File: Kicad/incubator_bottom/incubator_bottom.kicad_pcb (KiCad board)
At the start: 2 copper layers, 100.1 x 73.7 mm, 38 parts, among them J1 Conn_01x02, J2 Conn_02x03_Odd_Even, J3 RJ12, J4 Conn_01x05, J5 AudioJack3_SwitchTR, J6 AudioJack3_SwitchTR, J7 Conn_01x02, J8 Conn_01x06, Q1 ZXMS6004, Q2 IPB80N03S4L-03, U1 DS18B20Z, U2 DS18B20, U3 ATmega328P-AU

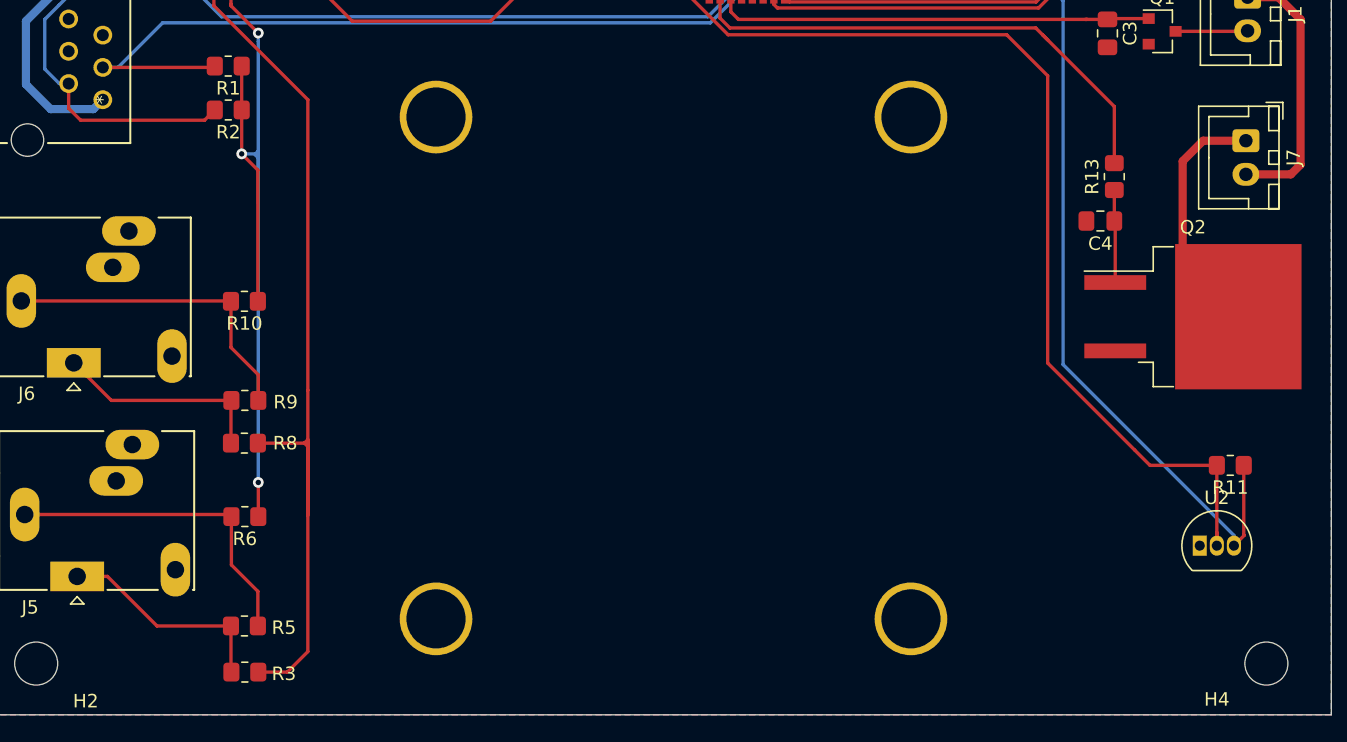
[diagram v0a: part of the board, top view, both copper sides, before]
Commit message: fix: Power resistor size
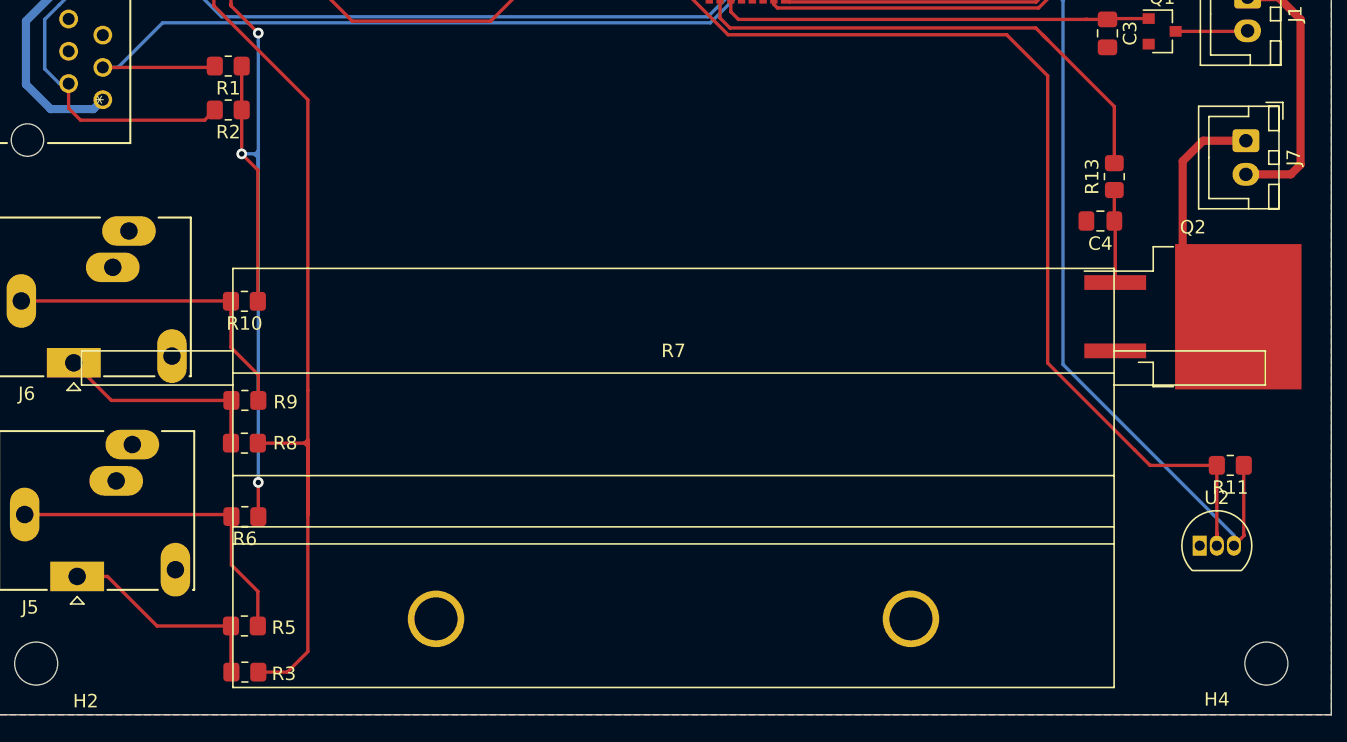
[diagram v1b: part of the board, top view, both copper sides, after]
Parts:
- R7: footprint Incubator:HSC1004R0J -> Incubator:100W4RJ; moved to F.Cu

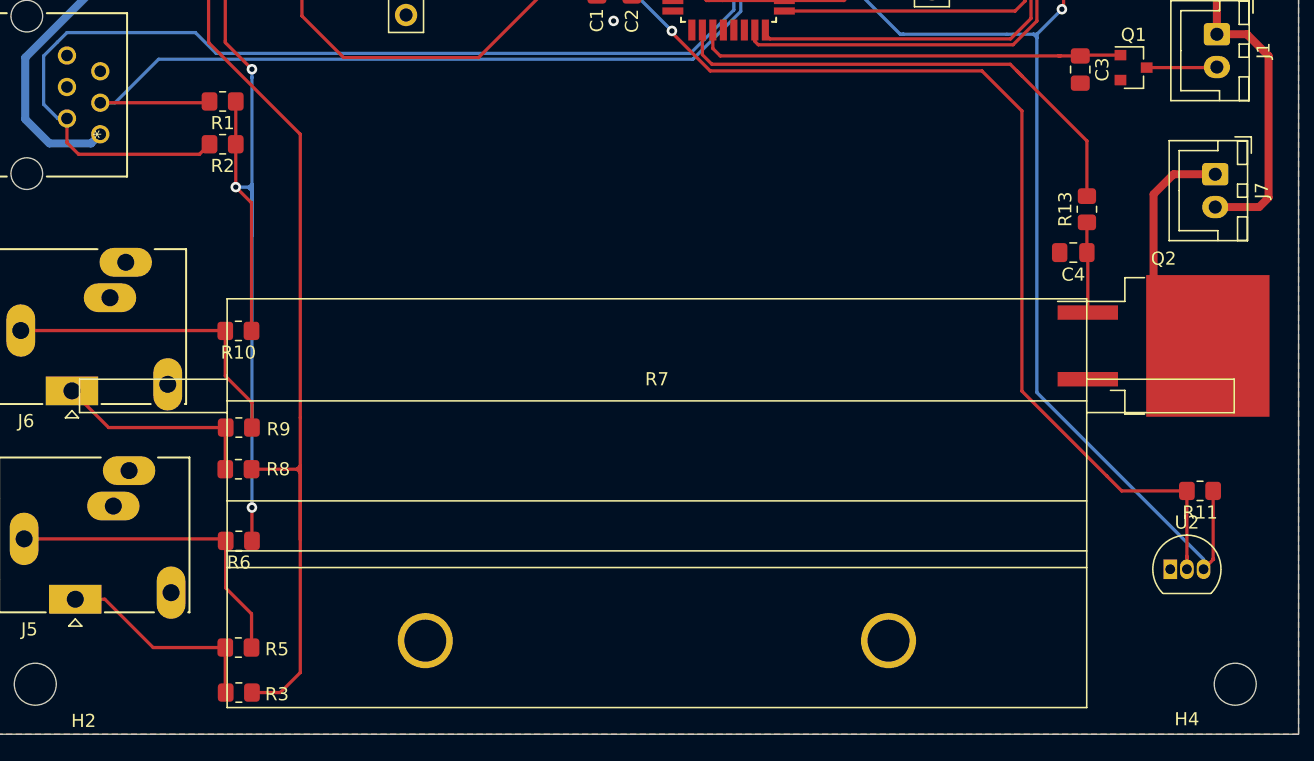
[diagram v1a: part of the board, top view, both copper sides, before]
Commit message: fix: Power resistor size and position
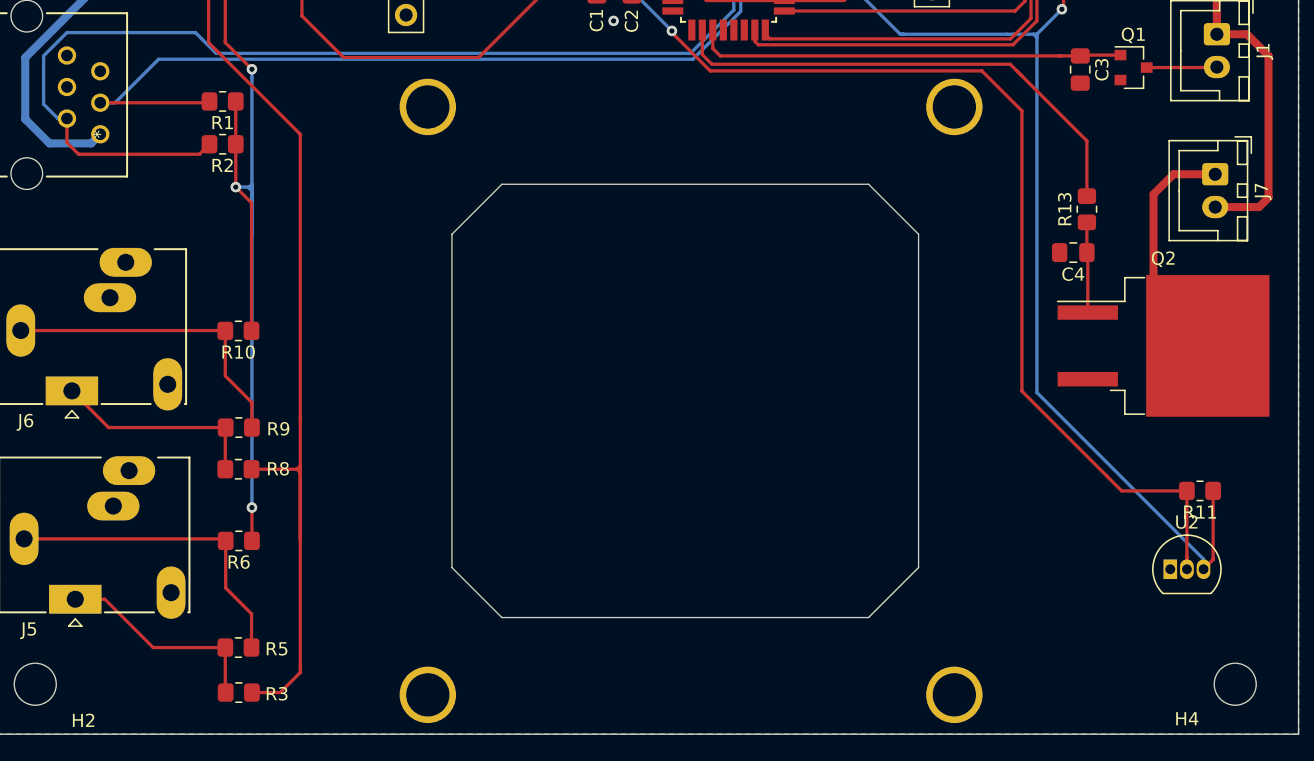
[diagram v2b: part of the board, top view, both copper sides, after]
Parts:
- added R15: 100W4RJ, Incubator:100W4RJ, B.Cu at (63.2, -25.4)
- R7: value HSC1004R0J -> 100W4RJ; moved to B.Cu
- moved R7 6.87 mm to (44.3, -25.4), turned to 90 degrees
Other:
- outline, holes or cut-outs redrawn

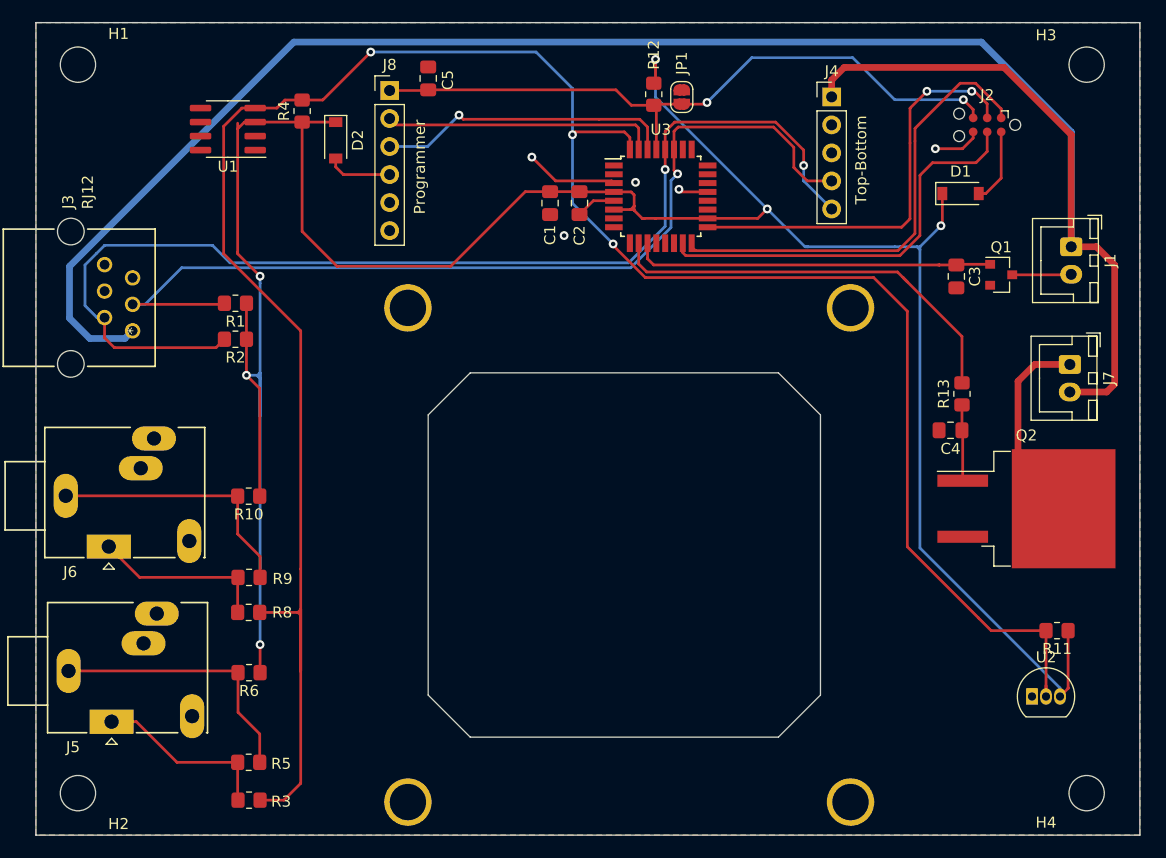
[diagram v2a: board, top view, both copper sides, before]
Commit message: fix: fan connection
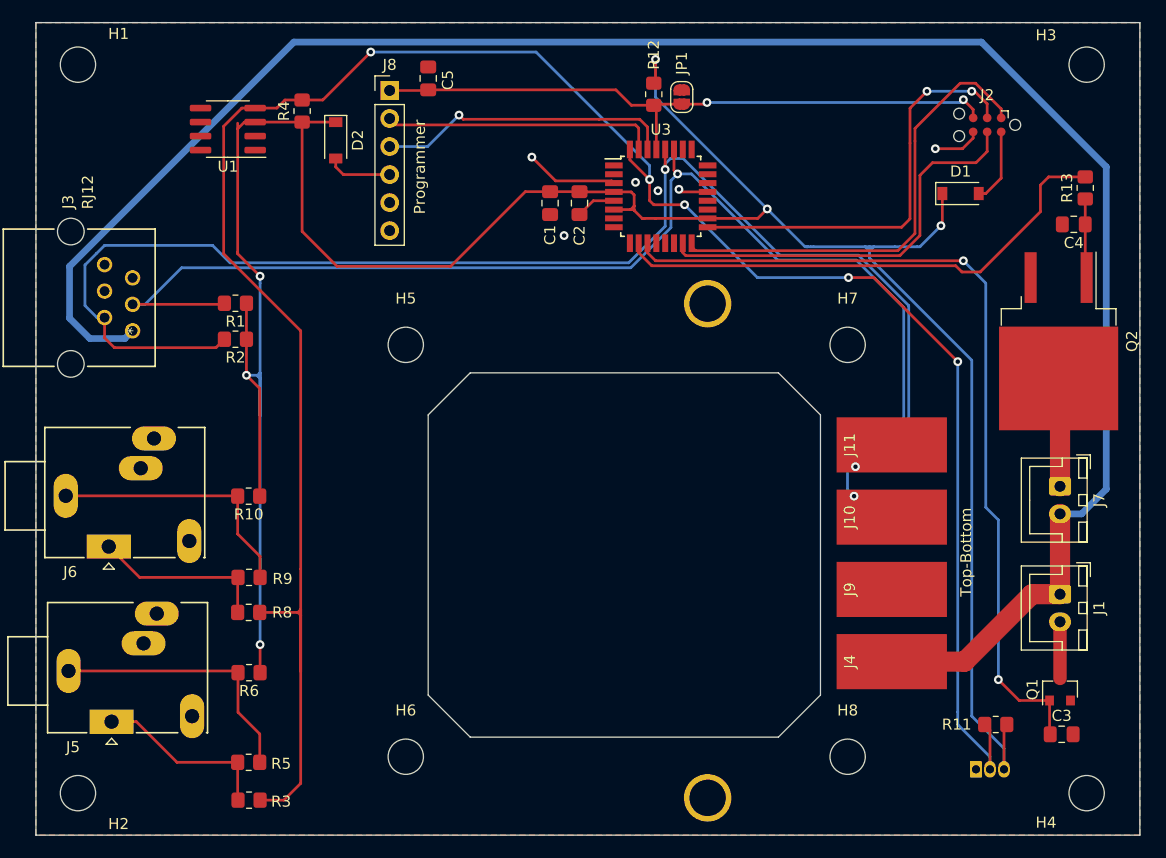
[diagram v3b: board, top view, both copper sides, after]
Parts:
- removed R15: 100W4RJ, Incubator:100W4RJ
- added H5: MountingHole, MountingHole:MountingHole_3.2mm_M3, F.Cu at (33.5, -44.5)
- added H6: MountingHole, MountingHole:MountingHole_3.2mm_M3, F.Cu at (33.5, -7.11)
- added H7: MountingHole, MountingHole:MountingHole_3.2mm_M3, F.Cu at (73.6, -44.5)
- added H8: MountingHole, MountingHole:MountingHole_3.2mm_M3, F.Cu at (73.6, -7.11)
- added J10: Conn_01x01, Connector_Wire:SolderWirePad_1x01_SMD_5x10mm, F.Cu at (77.6, -28.8)
- added J11: Conn_01x01, Connector_Wire:SolderWirePad_1x01_SMD_5x10mm, F.Cu at (77.6, -35.4)
- added J9: Conn_01x01, Connector_Wire:SolderWirePad_1x01_SMD_5x10mm, F.Cu at (77.6, -22.3)
- J4: value Conn_01x05 -> Conn_01x01; footprint Connector_PinHeader_2.54mm:PinHeader_1x05_P2.54mm_Vertical -> Connector_Wire:SolderWirePad_1x01_SMD_5x10mm
- U2: moved to B.Cu
- moved J4 51.5 mm to (77.6, -15.7), turned to 90 degrees
- moved C3 42.6 mm to (93.0, -9.14), turned to 0 degrees
- moved Q1 38.0 mm to (92.8, -13.2), turned to 90 degrees
- moved J1 31.5 mm to (92.8, -21.8)
- moved C4 21.8 mm to (94.1, -55.4)
- moved R13 21.8 mm to (95.1, -58.7)
- moved Q2 15.5 mm to (92.7, -44.8), turned to 270 degrees
- moved J7 11.1 mm to (92.8, -31.6)
- moved R11 10.2 mm to (87.0, -10.0)
- moved U2 8.33 mm to (85.2, -5.97)
- moved R7 5.98 mm to (50.3, -25.8), turned to 270 degrees
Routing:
- net FAN: track 32.9 -> 77.6 mm, vias 0 -> 2
- net SDA: track 86.7 -> 114.9 mm, vias 1 -> 2
- net SCL: track 103.6 -> 129.0 mm
- net Net-(J7-Pad1): track 18.6 -> 9.83 mm
- net PID: track 38.7 -> 47.0 mm
- net VIN: track 238.3 -> 242.8 mm
- net ~RESET: track 62.1 -> 58.9 mm
- net 12V: track 180.7 -> 178.0 mm
- net ONE-WIRE: track 207.9 -> 205.3 mm, vias 3 -> 5
- net GND: vias 5 -> 6

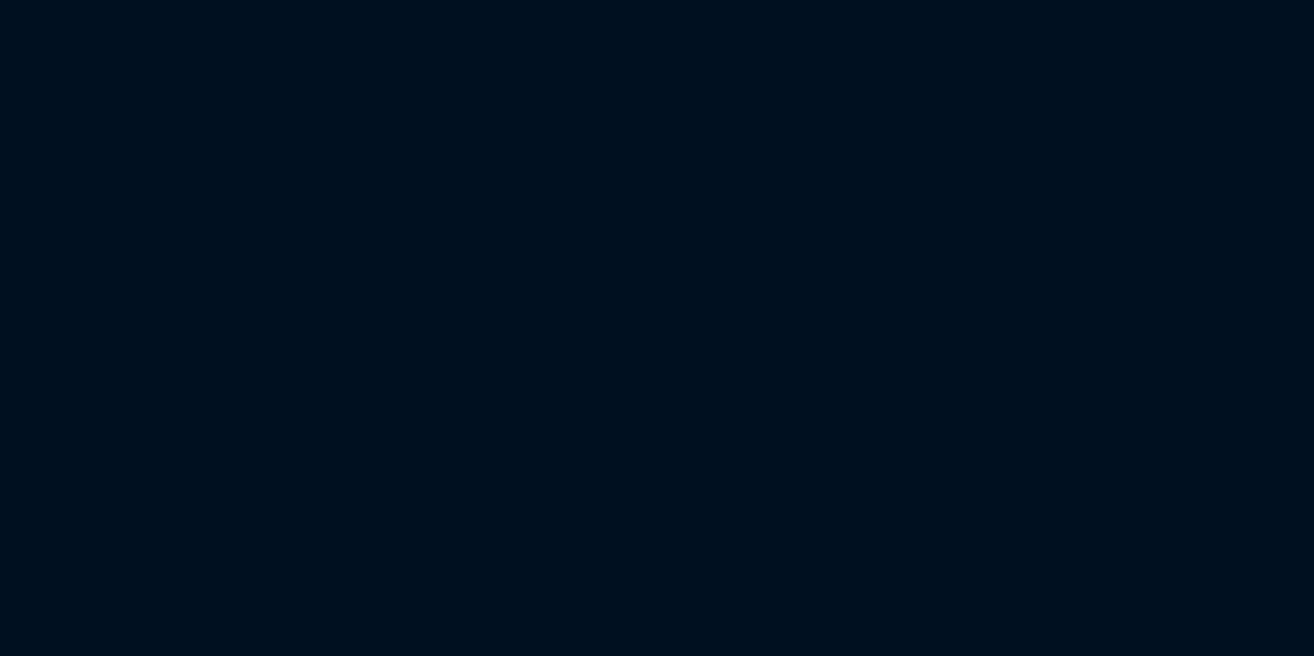
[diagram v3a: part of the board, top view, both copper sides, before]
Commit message: refactor:Step-down IC was changed
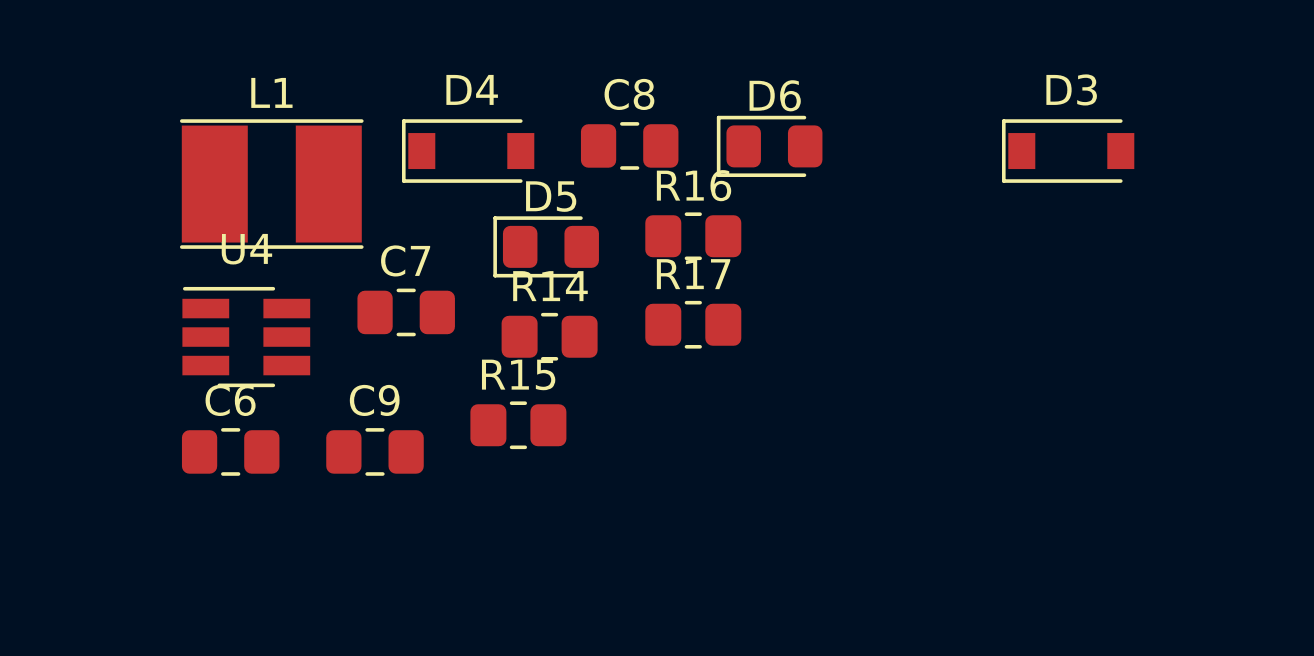
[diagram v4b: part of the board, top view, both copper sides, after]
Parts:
- added C6: 10µF, Capacitor_SMD:C_0805_2012Metric_Pad1.18x1.45mm_HandSolder, F.Cu at (31.5, -80.6)
- added C7: 22nF, Capacitor_SMD:C_0805_2012Metric_Pad1.18x1.45mm_HandSolder, F.Cu at (37.3, -85.3)
- added C8: 22µF, Capacitor_SMD:C_0805_2012Metric_Pad1.18x1.45mm_HandSolder, F.Cu at (44.8, -90.8)
- added C9: 22µF, Capacitor_SMD:C_0805_2012Metric_Pad1.18x1.45mm_HandSolder, F.Cu at (36.3, -80.6)
- added D3: MBR0520LT, Diode_SMD:D_SOD-123, F.Cu at (59.5, -90.7)
- added D4: MBR0520LT, Diode_SMD:D_SOD-123, F.Cu at (39.5, -90.7)
- added D5: GREEN, LED_SMD:LED_0805_2012Metric_Pad1.15x1.40mm_HandSolder, F.Cu at (42.2, -87.5)
- added D6: GREEN, LED_SMD:LED_0805_2012Metric_Pad1.15x1.40mm_HandSolder, F.Cu at (49.6, -90.8)
- added L1: 4.7µH, Inductor_SMD:L_Taiyo-Yuden_NR-40xx_HandSoldering, F.Cu at (32.9, -89.6)
- added R14: 9.64k, Resistor_SMD:R_0805_2012Metric_Pad1.20x1.40mm_HandSolder, F.Cu at (42.1, -84.5)
- added R15: 49.9k, Resistor_SMD:R_0805_2012Metric_Pad1.20x1.40mm_HandSolder, F.Cu at (41.1, -81.5)
- added R16: 10k, Resistor_SMD:R_0805_2012Metric_Pad1.20x1.40mm_HandSolder, F.Cu at (46.9, -87.8)
- added R17: 1k, Resistor_SMD:R_0805_2012Metric_Pad1.20x1.40mm_HandSolder, F.Cu at (46.9, -84.9)
- added U4: ACT4088, Package_TO_SOT_SMD:SOT-23-6_Handsoldering, F.Cu at (32.0, -84.5)

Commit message: refactor:rotated layer
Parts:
- C1, C2, C3, C4, C5, C6, C7, C8, C9, D1, D2, D3, D4, D5, D6, H1, H2, H3, H4, H5, H6, H7, H8, J1, J10, J11, J2, J3, J4, J5, J6, J7, J8, J9, JP1, L1, Q1, Q2, R1, R10, R11, R12, R13, R14, R15, R16, R17, R2, R3, R4, R5, R6, R8, R9, U1, U3, U4: moved to B.Cu
- R7, U2: moved to F.Cu
- moved C8 125.0 mm to (44.8, 34.2)
- moved D6 125.0 mm to (49.6, 34.2)
- moved D3 124.7 mm to (59.5, 34.0)
- moved D4 124.7 mm to (39.5, 34.0)
- moved L1 122.5 mm to (32.9, 32.9)
- moved R16 119.0 mm to (46.9, 31.2)
- moved D5 118.3 mm to (42.2, 30.8)
- moved C7 113.9 mm to (37.3, 28.7)
- moved R17 113.1 mm to (46.9, 28.2)
- moved R14 112.3 mm to (42.1, 27.8)
- moved U4 112.3 mm to (32.0, 27.8)
- moved R15 106.4 mm to (41.1, 24.9)
- moved C6 104.6 mm to (31.5, 24.0)
- moved C9 104.6 mm to (36.3, 24.0)
- moved H1 83.1 mm to (3.81, 13.2)
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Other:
- outline, holes or cut-outs redrawn

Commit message: test: power resistor
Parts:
- C1, C2, C3, C4, C5, C6, C7, C8, C9, D1, D2, D3, D4, D5, D6, H1, H2, H3, H4, H5, H6, H7, H8, J1, J10, J11, J2, J3, J4, J5, J6, J7, J8, J9, JP1, L1, Q1, Q2, R1, R10, R11, R12, R13, R14, R15, R16, R17, R2, R3, R4, R5, R6, R8, R9, U1, U3, U4: moved to F.Cu
- R7, U2: moved to B.Cu
- moved R3 190.1 mm to (87.4, 124.1)
- moved H2 189.0 mm to (71.9, 123.4)
- moved H4 189.0 mm to (163.3, 123.4)
- moved U2 184.9 mm to (153.3, 121.3)
- moved R5 183.8 mm to (87.4, 120.7)
- moved H6 182.8 mm to (101.6, 120.1)
- moved H8 182.8 mm to (141.7, 120.1)
- moved C3 179.1 mm to (161.1, 118.1)
- moved R11 177.4 mm to (155.1, 117.2)
- moved J5 176.9 mm to (74.9, 117.0)
- moved Q1 171.6 mm to (160.9, 114.0), turned to 90 degrees
- moved R6 168.8 mm to (87.4, 112.5)
- moved J4 166.9 mm to (145.7, 111.5), turned to 90 degrees
- moved R8 158.8 mm to (87.4, 107.1)
- moved J1 155.9 mm to (160.9, 105.4), turned to 270 degrees
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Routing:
- net VIN: track 242.8 -> 242.3 mm
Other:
- outline, holes or cut-outs redrawn
